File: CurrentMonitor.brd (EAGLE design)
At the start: 85 x 45 mm, 57 parts, among them J1 Ext Pwr, U1 NCP1117DT50G, U2 MCP1700T-3302E/TT, U3 ATmega328P-PU, Y1 16MHz 18pF

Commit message: Change Run/Pgm header to "lock" package.
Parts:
- JP3: device SparkFun:1X03 -> SparkFun:1X03_LOCK
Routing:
- net PD7: track 24.3 -> 23.4 mm
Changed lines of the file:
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@@
 <attribute name="VALUE" x="57.27" y="7.302" size="1.27" layer="27" font="vector" rot="R180"/>
 </element>
-<element name="JP3" library="SparkFun" package="1X03" value="Run/Pgm" x="10.5" y="4" smashed="yes">
+<element name="JP3" library="SparkFun" package="1X03_LOCK" value="Run/Pgm" x="10.5" y="4" smashed="yes">
 <attribute name="VALUE" x="9.23" y="0.825" size="1.27" layer="27"/>
 </element>
@@
 <wire x1="12.293" y1="43" x2="14.42" y2="40.873" width="0.3048" layer="1"/>
 <wire x1="27.5" y1="34.3" x2="27.5" y2="36.05" width="0.3048" layer="1"/>
-<wire x1="74.95" y1="26.7" x2="75.8" y2="26.7" width="0.4064" layer="1"/>
-<wire x1="75.8" y1="26.7" x2="76.5" y2="26" width="0.4064" layer="1"/>
-<wire x1="76.5" y1="26" x2="77.5" y2="26" width="0.4064" layer="1"/>
+<wire x1="76.4" y1="26" x2="77.5" y2="26" width="0.4064" layer="1"/>
 <wire x1="77.5" y1="26" x2="78" y2="25.5" width="0.4064" layer="1"/>
+<wire x1="76.4" y1="26" x2="76.1" y2="26.3" width="0.4064" layer="1"/>
+<wire x1="76.1" y1="26.3" x2="75.35" y2="26.3" width="0.4064" layer="1"/>
+<wire x1="75.35" y1="26.3" x2="74.95" y2="26.7" width="0.4064" layer="1"/>
 </signal>
 <signal name="RST">
@@
 <wire x1="39.9" y1="15.1" x2="35.9" y2="15.1" width="0.3048" layer="1"/>
 <wire x1="35.9" y1="15.1" x2="35.22" y2="15.78" width="0.3048" layer="1"/>
-<wire x1="13.04" y1="4" x2="14.54" y2="2.5" width="0.3048" layer="16"/>
+<wire x1="13.04" y1="3.873" x2="14.54" y2="2.5" width="0.3048" layer="16"/>
 <wire x1="14.54" y1="2.5" x2="47" y2="2.5" width="0.3048" layer="16"/>
 <wire x1="47" y1="2.5" x2="48.38" y2="3.88" width="0.3048" layer="16"/>
@@
 <contactref element="A1" pad="2"/>
 <wire x1="10.46" y1="9.32" x2="10.46" y2="4.04" width="0.3048" layer="1"/>
-<wire x1="10.46" y1="4.04" x2="10.5" y2="4" width="0.3048" layer="1"/>
+<wire x1="10.46" y1="4.04" x2="10.5" y2="4.127" width="0.3048" layer="1"/>
 </signal>
 <signal name="N$8">
@@
 <contactref element="TB6" pad="P$1"/>
 <contactref element="U3" pad="13"/>
-<wire x1="63.16" y1="17.67" x2="63.16" y2="22.44" width="0.3048" layer="16"/>
-<wire x1="63.16" y1="22.44" x2="61.9" y2="23.7" width="0.3048" layer="16"/>
-<wire x1="61.9" y1="23.7" x2="61.9" y2="32.2" width="0.3048" layer="16"/>
-<wire x1="61.9" y1="32.2" x2="67.5" y2="37.8" width="0.3048" layer="16"/>
-<wire x1="67.5" y1="37.8" x2="67.5" y2="38.75" width="0.3048" layer="16"/>
-<wire x1="67.5" y1="38.75" x2="67.75" y2="39" width="0.3048" layer="16"/>
+<wire x1="63.16" y1="17.67" x2="63.16" y2="22.16" width="0.3048" layer="16"/>
+<wire x1="63.16" y1="22.16" x2="64.5" y2="23.5" width="0.3048" layer="16"/>
+<wire x1="64.5" y1="23.5" x2="64.5" y2="35" width="0.3048" layer="16"/>
+<wire x1="64.5" y1="35" x2="68" y2="38.5" width="0.3048" layer="16"/>
+<wire x1="68" y1="38.5" x2="68" y2="38.75" width="0.3048" layer="16"/>
+<wire x1="68" y1="38.75" x2="67.75" y2="39" width="0.3048" layer="16"/>
 </signal>
 <signal name="N$9">

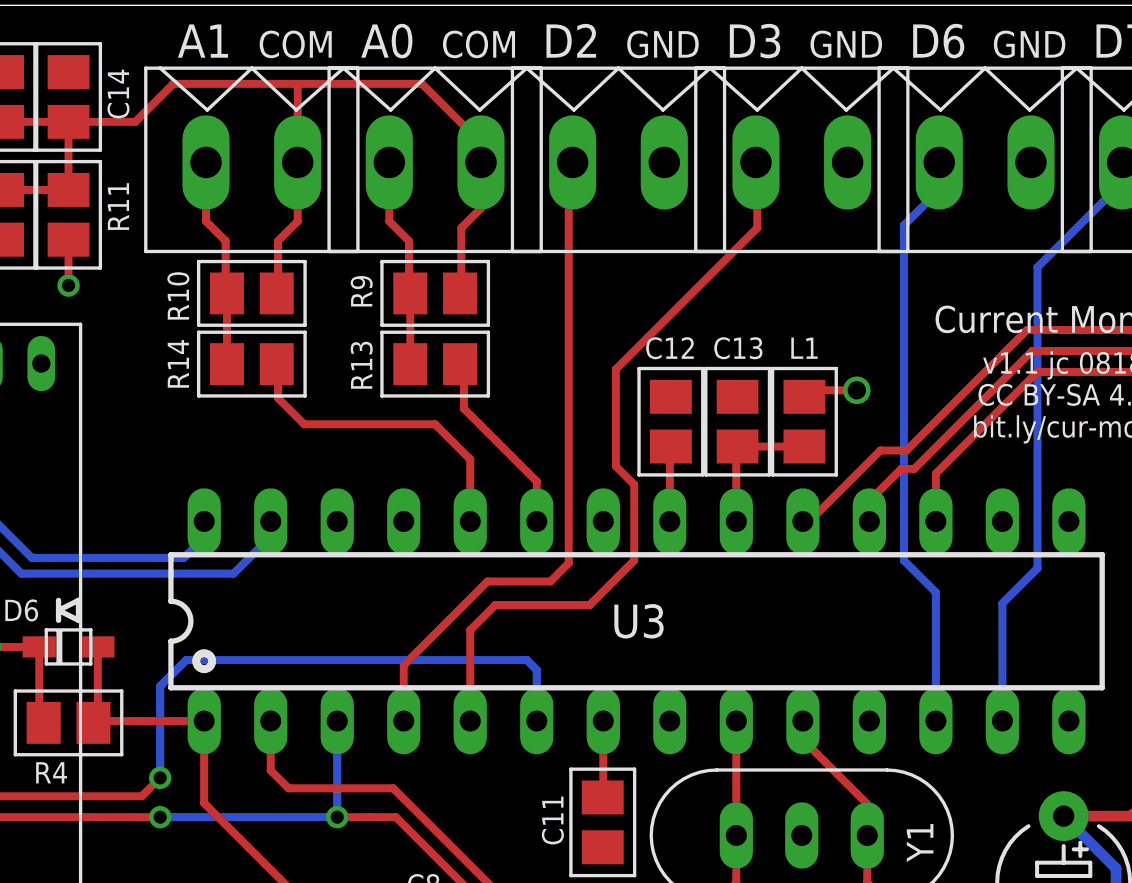
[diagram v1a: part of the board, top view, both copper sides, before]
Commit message: Minor board layout tweaks.
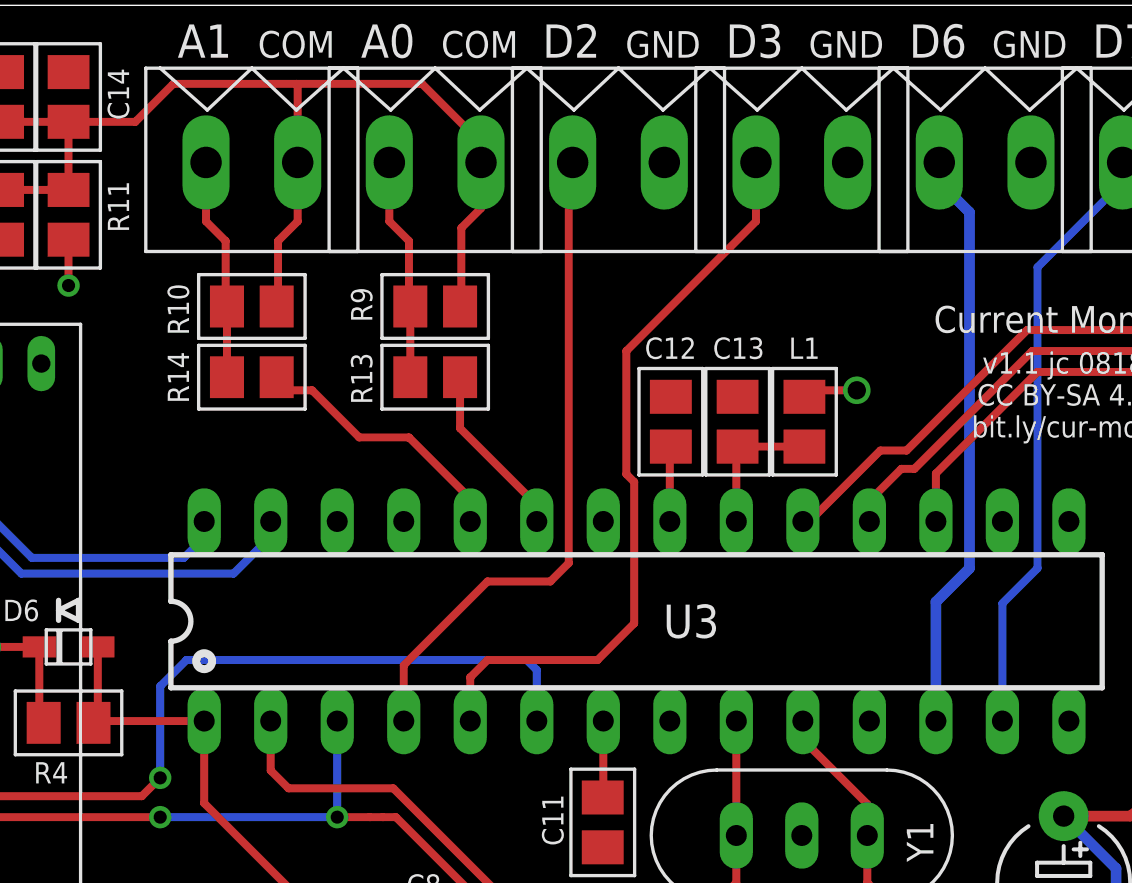
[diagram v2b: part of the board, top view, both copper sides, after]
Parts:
- moved LOGO2 1.00 mm to (34.5, 32.5)
- moved R10 0.50 mm to (34.5, 33.5)
- moved R13 0.50 mm to (41.5, 30.8)
- moved R14 0.50 mm to (34.5, 30.8)
- moved R9 0.50 mm to (41.5, 33.5)
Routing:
- net ADC1: track 12.0 -> 10.2 mm
- net N$3: track 39.3 -> 40.3 mm
